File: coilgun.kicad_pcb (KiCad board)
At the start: 2 copper layers, 89.3 x 63.5 mm, 43 parts, among them J1 Conn_01x02, J2 Conn_02x05_Odd_Even, J3 Conn_02x05_Odd_Even, J4 Conn_01x03, J5 Conn_01x03, J6 Conn_01x02, J7 Conn_01x02, J8 Conn_01x02, Q1 BC547, Q2 BC558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

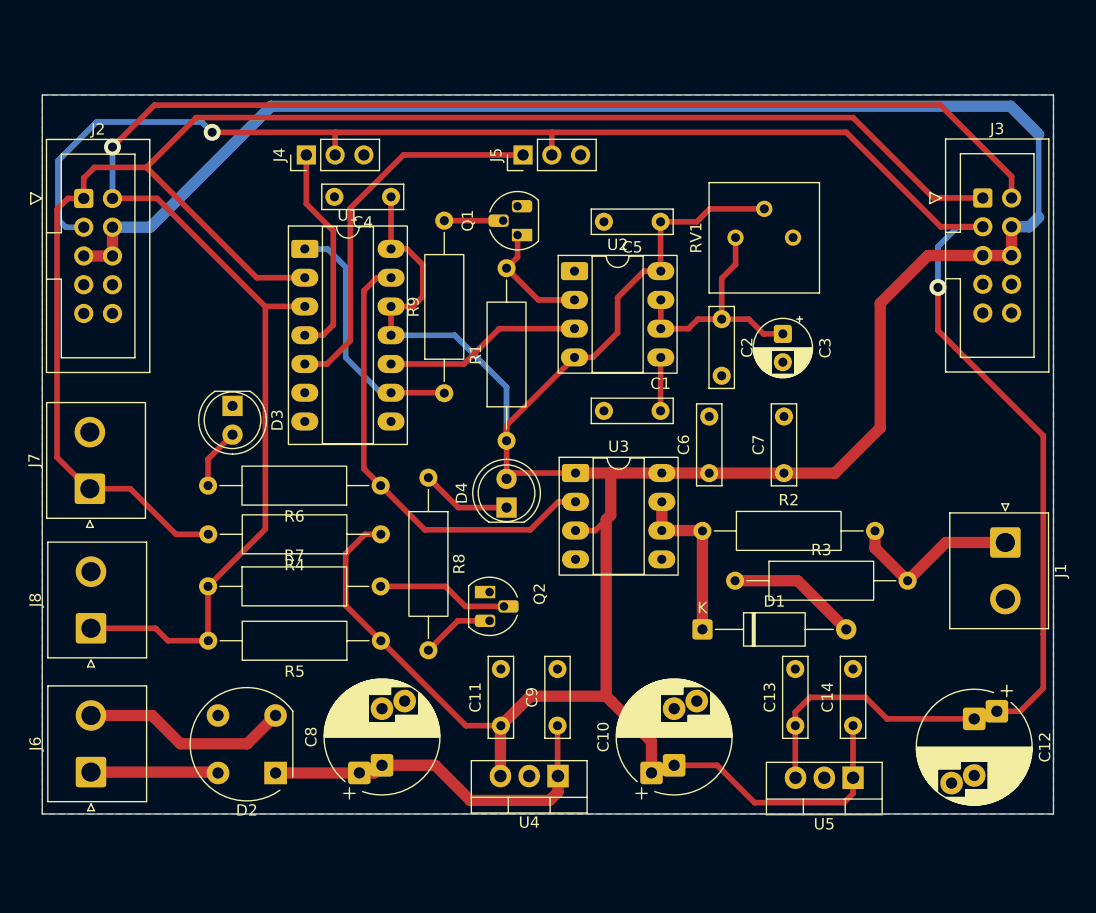
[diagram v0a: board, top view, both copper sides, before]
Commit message: Fix bugs and label placement
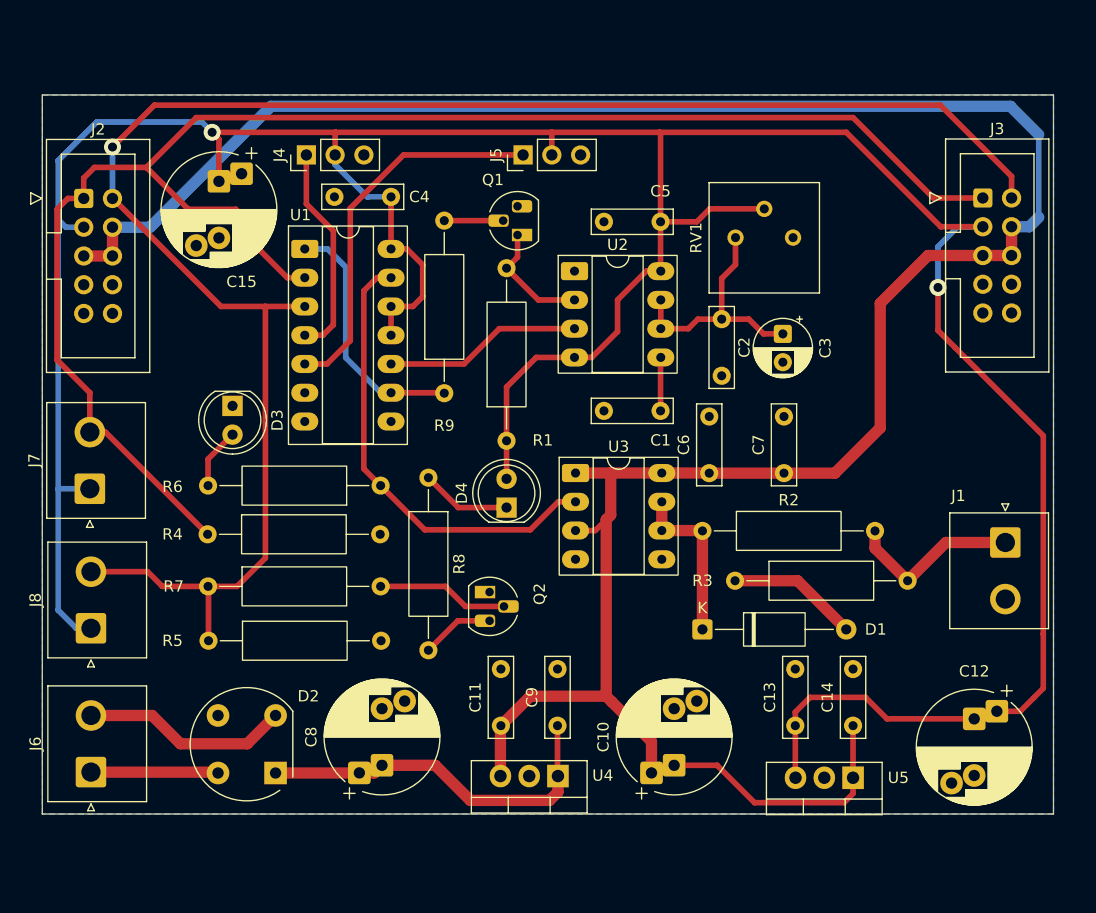
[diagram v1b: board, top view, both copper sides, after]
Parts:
- added C15: 1000uF, Capacitor_THT:CP_Radial_D10.0mm_P5.00mm_P7.50mm, F.Cu at (84.1, 35.8)
- C1: value C -> 10nF
- C3: value C_Polarized -> 1uF
- C4, C5, C6: value C -> 100nF
- C7: value C_Polarized -> 10uF Tantal
- D1: value D_Schottky -> 1n5819
- R1, R4, R5, R7, R9: value R -> 10K
- R2, R3: value R -> 10R
- RV1: value R_Potentiometer -> 100K
- moved R4 15.3 mm to (83.1, 67.0), turned to 0 degrees
- moved R5 15.2 mm to (83.2, 76.4), turned to 0 degrees
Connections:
- C4 pad 1: VDD -> +5V
- C5 pad 1: VDD -> +5V
- D4 pad 2: VDD -> +5V
- J7 pad 1: TRIGGER -> +5V
- J7 pad 2: GND -> TRIGGER
- J8 pad 1: SAFETY -> +5V
- J8 pad 2: GND -> SAFETY
- R1 pad 1: VDD -> +5V
- R4 pad 1: VDD -> TRIGGER
- R4 pad 2: TRIGGER -> GND
- R5 pad 1: VDD -> SAFETY
- R5 pad 2: SAFETY -> GND
- RV1 pad 2: VDD -> +5V
- U1 pad 11: VDD -> +5V
- U1 pad 12: VDD -> +5V
- U1 pad 14: VDD -> +5V
- U2 pad 4: VDD -> +5V
- U2 pad 8: VDD -> +5V
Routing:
- net +5V: track 176.3 -> 297.2 mm
- net VDD: track 353.5 -> 247.6 mm
- net TRIGGER: track 145.2 -> 143.0 mm
- net SAFETY: track 153.4 -> 154.9 mm

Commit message: Release 08.12.2025
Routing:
- net +5V: track 297.2 -> 299.2 mm
- net TRIGGER: track 143.0 -> 144.0 mm
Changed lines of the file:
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@@
 			(outputformat 1)
 			(mirror no)
-			(drillshape 1)
+			(drillshape 0)
 			(scaleselection 1)
-			(outputdirectory "")
+			(outputdirectory "gerber/")
 		)
 	)
@@
 	)
 	(segment
-		(start 134 61.6)
-		(end 138.5 61.6)
-		(width 1)
-		(layer "F.Cu")
-		(net 4)
-	)
-	(segment
 		(start 108.96 83.94)
 		(end 109 83.9)
@@
 	)
 	(segment
-		(start 118.7 61.59)
-		(end 115.59 61.59)
+		(start 142.5 57.6)
+		(end 138.5 61.6)
 		(width 1)
 		(layer "F.Cu")
@@
 	)
 	(segment
-		(start 142.5 57.6)
-		(end 142.5 46.6)
+		(start 118.7 61.59)
+		(end 115.59 61.59)
 		(width 1)
 		(layer "F.Cu")
@@
 	)
 	(segment
-		(start 138.4 61.7)
-		(end 138.5 61.6)
-		(width 0.5)
+		(start 142.5 57.6)
+		(end 142.5 46.6)
+		(width 1)
 		(layer "F.Cu")
 		(net 4)
@@
 	(segment
 		(start 138.5 61.6)
-		(end 142.5 57.6)
+		(end 134 61.6)
 		(width 1)
 		(layer "F.Cu")
@@
 	)
 	(segment
-		(start 74.7 39.88)
-		(end 78.02 39.88)
+		(start 76.02 39.88)
+		(end 86.699 29.201)
 		(width 1)
 		(layer "B.Cu")
@@
 	)
 	(segment
-		(start 78.02 39.88)
-		(end 88.699 29.201)
+		(start 86.699 29.201)
+		(end 154.001 29.201)
 		(width 1)
 		(layer "B.Cu")
@@
 	)
 	(segment
-		(start 88.699 29.201)
-		(end 154.001 29.201)
+		(start 74.7 39.88)
+		(end 76.02 39.88)
 		(width 1)
 		(layer "B.Cu")
@@
 	)
 	(segment
+		(start 81.501471 31.498529)
+		(end 83.498529 31.498529)
+		(width 0.5)
+		(layer "F.Cu")
+		(net 6)
+	)
+	(segment
 		(start 109.5 54)
 		(end 112.12 51.38)
@@
 	)
 	(segment
+		(start 84.1 32.1)
+		(end 84.1 35.827856)
+		(width 0.5)
+		(layer "F.Cu")
+		(net 6)
+	)
+	(segment
 		(start 139.5 31.5)
 		(end 147.84 39.84)
@@
 	)
 	(segment
+		(start 81.5 31.5)
+		(end 94.4 31.5)
+		(width 0.5)
+		(layer "F.Cu")
+		(net 6)
+	)
+	(segment
 		(start 156.9 80.6)
 		(end 156.9 75.8)
@@
 	)
 	(segment
-		(start 83.5 31.5)
-		(end 94.4 31.5)
-		(width 0.5)
-		(layer "F.Cu")
-		(net 6)
-	)
-	(segment
 		(start 152.8 82.627856)
 		(end 154.872144 82.627856)
@@
 	)
 	(segment
-		(start 84.1 32.1)
-		(end 83.5 31.5)
+		(start 123.1 31.6)
+		(end 123 31.5)
 		(width 0.5)
 		(layer "F.Cu")
@@
 	)
 	(segment
-		(start 84.1 35.827856)
+		(start 83.498529 31.498529)
 		(end 84.1 32.1)
 		(width 0.5)
@@
 	)
 	(segment
-		(start 123.1 31.6)
-		(end 123 31.5)
-		(width 0.5)
-		(layer "F.Cu")
-		(net 6)
-	)
-	(segment
 		(start 126.3 39.4)
 		(end 127.44 38.26)
@@
 	)
 	(segment
+		(start 81.5 31.5)
+		(end 81.501471 31.498529)
+		(width 0.5)
+		(layer "F.Cu")
+		(net 6)
+	)
+	(segment
 		(start 109.5 62.1)
 		(end 109.5 58.74)
@@
 	)
 	(via
-		(at 83.5 31.5)
+		(at 81.5 31.5)
 		(size 1.5)
 		(drill 0.8)
@@
 	)
 	(segment
-		(start 69.9 34)
-		(end 69.9 39.2)
+		(start 80.6 30.6)
+		(end 73.3 30.6)
 		(width 0.5)
 		(layer "B.Cu")
@@
 	)
 	(segment
-		(start 69.9 39.2)
-		(end 70.58 39.88)
+		(start 73.3 30.6)
+		(end 69.9 34)
 		(width 0.5)
 		(layer "B.Cu")
@@
 	)
 	(segment
-		(start 83.5 31.5)
-		(end 82.6 30.6)
+		(start 69.9 39.2)
+		(end 70.58 39.88)
 		(width 0.5)
 		(layer "B.Cu")
@@
 	)
 	(segment
-		(start 97.2 37.2)
-		(end 94.36 34.36)
+		(start 81.5 31.5)
+		(end 80.6 30.6)
 		(width 0.5)
 		(layer "B.Cu")
@@
 	)
 	(segment
-		(start 82.6 30.6)
-		(end 73.3 30.6)
+		(start 97.2 37.2)
+		(end 94.36 34.36)
 		(width 0.5)
 		(layer "B.Cu")
@@
 	)
 	(segment
-		(start 73.3 30.6)
-		(end 69.9 34)
+		(start 69.9 34)
+		(end 69.9 39.2)
 		(width 0.5)
 		(layer "B.Cu")
@@
 	)
 	(segment
+		(start 151.56 37.3)
+		(end 147.2 37.3)
+		(width 0.5)
+		(layer "F.Cu")
+		(net 13)
+	)
+	(segment
 		(start 70.76 37.34)
 		(end 72.16 37.34)
@@
 	)
 	(segment
+		(start 80.5 30.2)
+		(end 77.7 33)
+		(width 0.5)
+		(layer "F.Cu")
+		(net 13)
+	)
+	(segment
 		(start 73.1 34.6)
 		(end 77.7 34.6)
@@
 	)
 	(segment
-		(start 151.56 37.3)
-		(end 147.2 37.3)
+		(start 147.2 37.3)
+		(end 140.1 30.2)
 		(width 0.5)
 		(layer "F.Cu")
@@
 	)
 	(segment
-		(start 82.1 30.2)
-		(end 77.7 34.6)
-		(width 0.5)
-		(layer "F.Cu")
-		(net 13)
-	)
-	(segment
 		(start 90.14 44.34)
 		(end 86.8 41)
@@
 	)
 	(segment
-		(start 147.2 37.3)
-		(end 140.1 30.2)
+		(start 72.7 57.9775)
+		(end 74.0775 57.9775)
 		(width 0.5)
 		(layer "F.Cu")
@@
 	)
 	(segment
-		(start 72.7 57.9775)
-		(end 74.0775 57.9775)
+		(start 140.1 30.2)
+		(end 80.5 30.2)
 		(width 0.5)
 		(layer "F.Cu")
@@
 	)
 	(segment
-		(start 140.1 30.2)
-		(end 82.1 30.2)
+		(start 72.7 57.9775)
+		(end 72.7 54.5)
 		(width 0.5)
 		(layer "F.Cu")
@@
 	)
 	(segment
-		(start 72.7 57.9775)
-		(end 72.7 54.5)
+		(start 91.68 44.34)
+		(end 90.14 44.34)
 		(width 0.5)
 		(layer "F.Cu")
@@
 	)
 	(segment
-		(start 91.68 44.34)
-		(end 90.14 44.34)
+		(start 77.7 33)
+		(end 77.7 34.6)
 		(width 0.5)
 		(layer "F.Cu")

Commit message: Fix error
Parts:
- added C16: 10uF, Capacitor_THT:CP_Radial_D5.0mm_P2.50mm, F.Cu at (114.0, 40.5)
- added C17: 100nF, Capacitor_THT:C_Rect_L7.0mm_W2.0mm_P5.00mm, F.Cu at (83.0, 47.0)
- added C18: 100nF, Capacitor_THT:C_Rect_L7.0mm_W2.0mm_P5.00mm, F.Cu at (86.0, 47.0)
- added H1: MountingHole_Pad, MountingHole:MountingHole_2.2mm_M2_Pad_Via, F.Cu at (154.0, 26.0)
- added H2: MountingHole_Pad, MountingHole:MountingHole_2.2mm_M2_Pad_Via, F.Cu at (154.0, 95.0)
- added H3: MountingHole_Pad, MountingHole:MountingHole_2.2mm_M2_Pad_Via, F.Cu at (73.0, 26.0)
- added H6: MountingHole_Pad, MountingHole:MountingHole_2.2mm_M2_Pad_Via, F.Cu at (73.0, 95.0)
- added R10: 10K, Resistor_THT:R_Axial_DIN0309_L9.0mm_D3.2mm_P15.24mm_Horizontal, F.Cu at (113.4, 58.8)
- Q2: value BC558 -> BC547
- moved C1 4.63 mm to (126.8, 53.2)
- moved C2 4.63 mm to (132.2, 45.1)
- moved C5 4.63 mm to (126.8, 36.5)
- moved U2 4.63 mm to (119.2, 40.9)
- moved C3 4.63 mm to (137.6, 46.5)
- moved RV1 4.63 mm to (138.4, 38.0)
- moved Q2 2.78 mm to (109.2, 74.6), turned to 90 degrees
- moved Q1 1.40 mm to (109.1, 40.6)
- moved C6 0.05 mm to (127.3, 61.6)
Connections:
- Q2 pad 1: GND -> Net-(Q2-C)
- Q2 pad 3: Net-(Q2-E) -> GND
- R8 pad 2: Net-(Q2-E) -> Net-(Q2-C)
- U2 pad 2: Net-(Q1-C) -> Net-(U2-TR)
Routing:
- net Net-(U2-TR): track 0.00 -> 8.97 mm
- net Net-(Q2-C): track 0.00 -> 7.66 mm
- net Net-(Q2-E): track 6.48 -> 0.00 mm
- net TRIGGER: track 144.0 -> 150.2 mm
- net +5V: track 299.2 -> 304.1 mm
- net Net-(U2-Q): track 17.5 -> 22.3 mm
- net SAFETY: track 154.9 -> 157.3 mm
- net Net-(Q1-C): track 10.5 -> 9.01 mm
- net Net-(Q1-B): track 5.20 -> 3.80 mm
- net Net-(Q2-B): track 11.6 -> 10.2 mm
- net VDD: track 247.5 -> 248.2 mm
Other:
- board size 89.3 x 63.5 mm -> 91.3 x 76.1 mm
- board text added: "FIRE"
- board text added: "G"
- board text added: "NEXT"
- board text added: "POWER"
- board text added: "PREV"
- board text added: "RDY"
- board text added: "S"
- board text added: "S+-"
- board text added: "SAFE"
- board text added: "TRG"

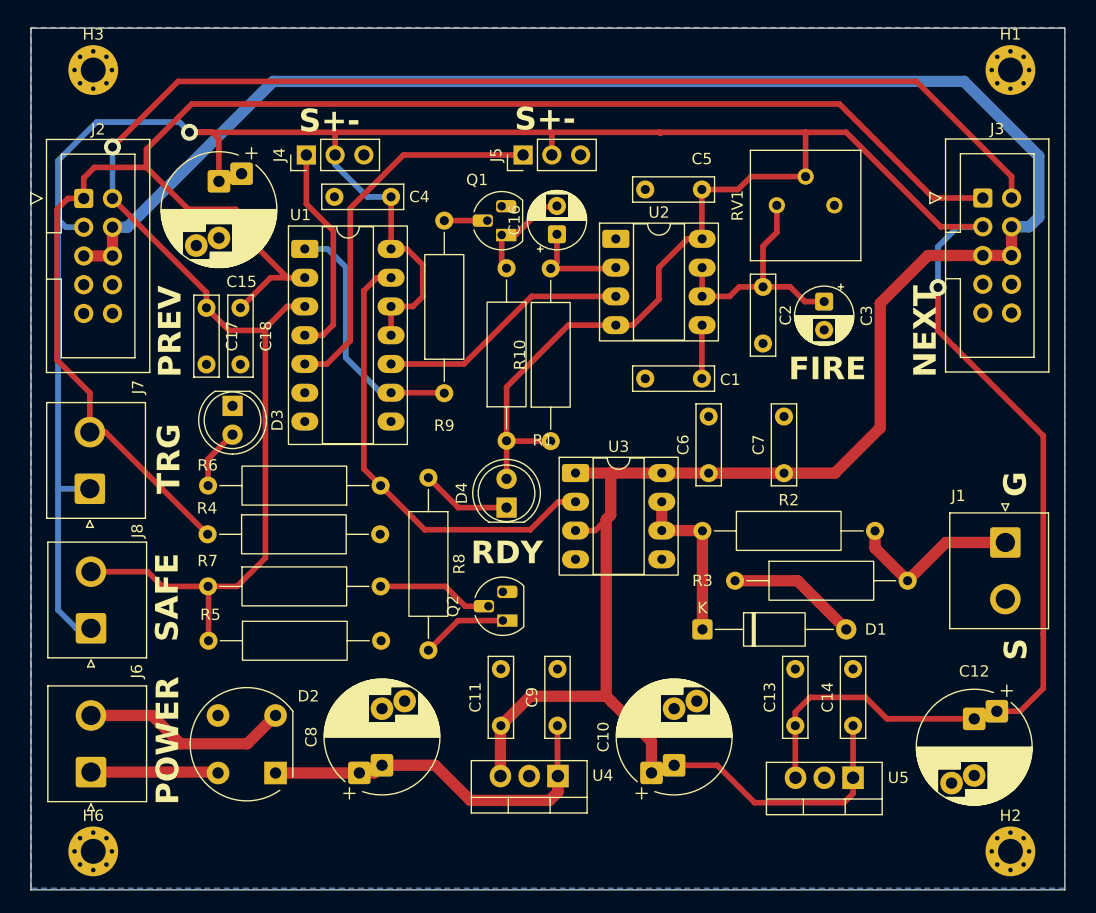
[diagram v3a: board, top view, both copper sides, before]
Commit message: safe led, fix 555 trigger, logos
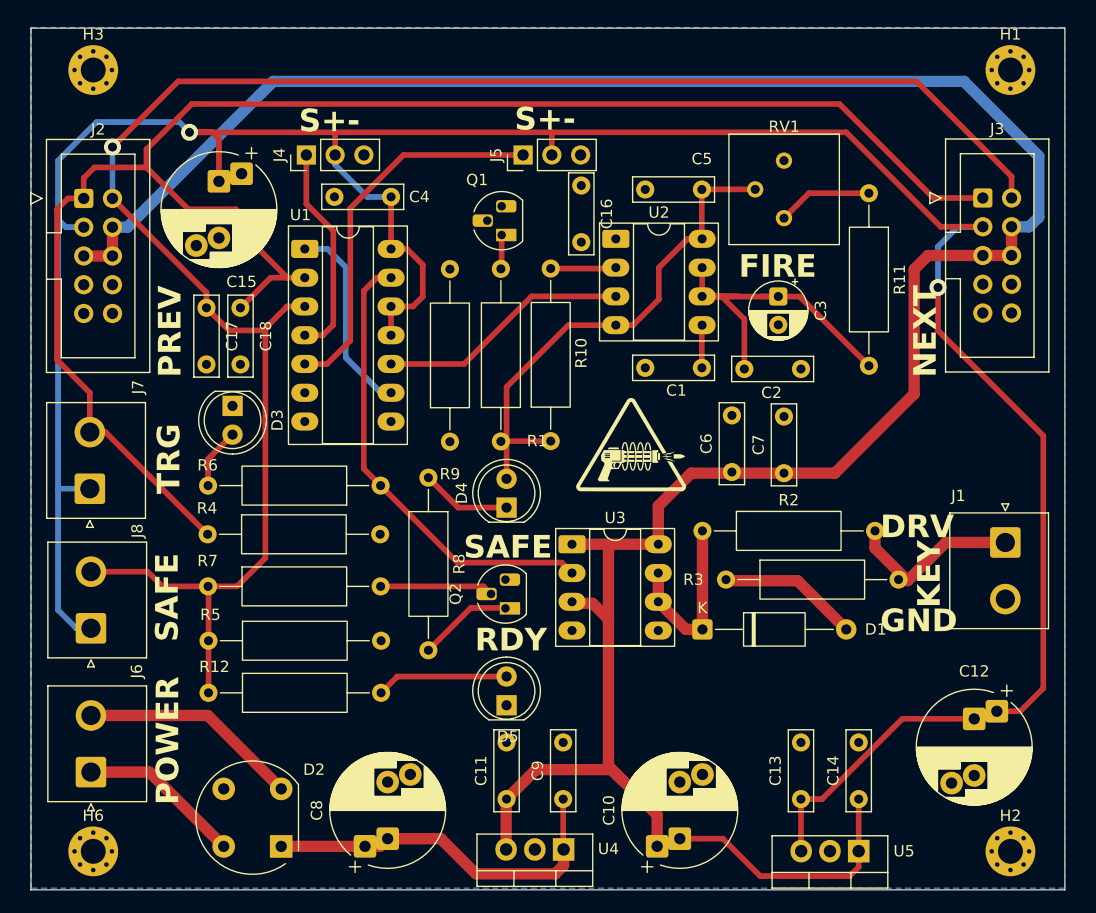
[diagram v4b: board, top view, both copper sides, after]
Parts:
- added D5: RED LED, LED_THT:LED_D5.0mm, F.Cu at (109.5, 82.1)
- added G***: LOGO, LOCAL:logo10x10, F.Cu at (120.5, 59.5)
- added G***: LOGO, LOCAL:logo20x20, B.Cu at (111.5, 53.5)
- added R11: 10K, Resistor_THT:R_Axial_DIN0309_L9.0mm_D3.2mm_P15.24mm_Horizontal, F.Cu at (141.5, 36.9)
- added R12: R, Resistor_THT:R_Axial_DIN0309_L9.0mm_D3.2mm_P15.24mm_Horizontal, F.Cu at (83.2, 81.0)
- C16: value 10uF -> 100nF; footprint Capacitor_THT:CP_Radial_D5.0mm_P2.50mm -> Capacitor_THT:C_Rect_L7.0mm_W2.0mm_P5.00mm
- D3: value LED -> WHITE LED
- D4: value LED -> GREEN LED
- Q2: value BC547 -> BC557
- moved C2 7.44 mm to (130.5, 52.4), turned to 0 degrees
- moved U4 6.50 mm to (114.5, 94.8)
- moved C10 6.50 mm to (124.8, 93.9)
- moved C11 6.50 mm to (109.5, 90.4)
- moved C13 6.50 mm to (135.5, 90.4)
- moved C14 6.50 mm to (140.6, 90.4)
- moved C8 6.50 mm to (99.0, 93.9)
- moved C9 6.50 mm to (114.5, 90.4)
- moved D2 6.50 mm to (89.6, 94.6)
- moved U5 6.50 mm to (140.6, 95.0)
- moved U3 6.30 mm to (115.3, 67.9)
- moved RV1 5.95 mm to (134.0, 34.0), turned to 180 degrees
- moved C16 4.81 mm to (116.1, 36.2), turned to -90 degrees
- moved R9 4.31 mm to (104.5, 58.8)
- moved C3 4.07 mm to (133.5, 46.0)
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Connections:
- C16 pad 1: Net-(U2-TR) -> Net-(Q1-C)
- C16 pad 2: Net-(Q1-C) -> Net-(U2-TR)
- RV1 pad 3: Net-(U2-DIS) -> Net-(R11-Pad1)
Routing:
- net Net-(U2-DIS): track 21.9 -> 35.9 mm
- net Net-(D5-A): track 0.00 -> 11.7 mm
- net +5V: track 304.1 -> 292.9 mm
- net VDD: track 248.2 -> 237.6 mm
- net Net-(R11-Pad1): track 0.00 -> 8.41 mm
- net Net-(Q1-C): track 9.01 -> 2.50 mm
- net Net-(R9-Pad1): track 22.3 -> 16.7 mm
- net SAFETY: track 157.3 -> 161.9 mm
- net Net-(Q1-B): track 3.80 -> 0.00 mm
- net Net-(U2-TR): track 8.97 -> 5.67 mm
- net Net-(J6-Pin_1): track 11.3 -> 14.4 mm
- net Net-(D1-K): track 14.8 -> 16.2 mm
- net Net-(J6-Pin_2): track 18.4 -> 19.5 mm
- net Net-(U2-CV): track 4.73 -> 3.75 mm
- net Net-(Q2-C): track 7.66 -> 8.37 mm
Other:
- board text added: "DRV"
- board text added: "GND"
- board text added: "KEY"
- board text removed: "G"
- board text removed: "S"

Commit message: updated
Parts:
- moved J5 4.96 mm to (106.0, 33.5)
- moved RV1 2.50 mm to (136.5, 34.0), turned to 90 degrees
- moved C16 0.92 mm to (115.5, 35.5)
- moved J4 0.53 mm to (92.0, 33.0)
- moved J1 0.50 mm to (154.1, 67.7)
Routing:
- net Net-(Q1-C): track 2.50 -> 11.8 mm
- net Net-(R9-Pad1): track 16.7 -> 23.7 mm
- net +5V: track 292.9 -> 298.8 mm
- net Net-(Q1-B): track 0.00 -> 5.65 mm
- net LASER2: track 33.8 -> 28.8 mm
- net Net-(U2-TR): track 5.67 -> 9.79 mm
- net Net-(R11-Pad1): track 8.41 -> 11.6 mm
- net LASER1: track 18.9 -> 19.5 mm
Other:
- board text added: "1 Sensor 2"
- board text added: "15V"
- board text added: "5V"
- board text added: "Key = S1 & S2 & Safe & TRG & <maxTime"
- board text added: "Max pulse len"
